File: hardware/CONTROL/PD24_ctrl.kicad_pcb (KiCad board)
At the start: 2 copper layers, 39.7 x 14 mm, 13 parts, among them J1 Conn_01x12_Socket, J2 Conn_01x08_Socket, SW1 SW_Push, SW2 SW_Push, SW3 SW_Push, U1 STM32G031G8Ux, U2 ips_0.96_16080, U3 TPS54202DDC, U4 INA228

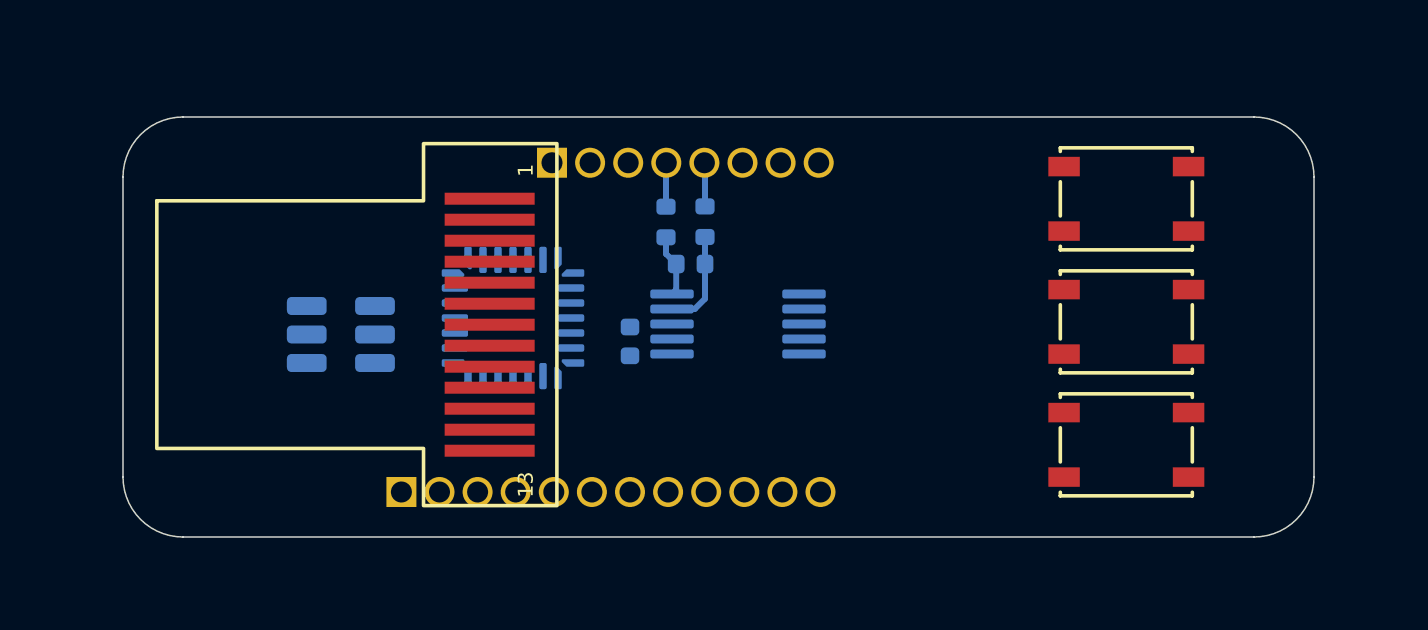
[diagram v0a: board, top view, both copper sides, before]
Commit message: PD24 控制部分的PCB设计完成
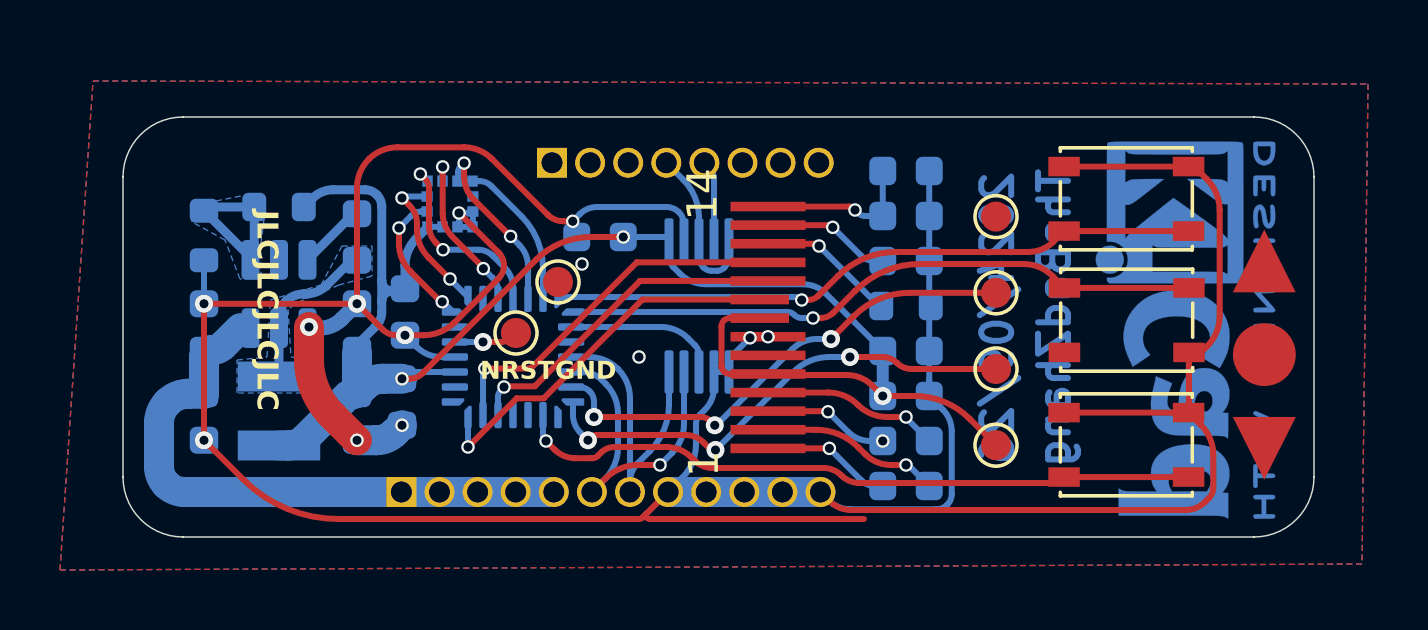
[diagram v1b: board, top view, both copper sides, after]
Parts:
- removed R6: 68R, Resistor_SMD:R_0402_1005Metric
- removed the U2 at (149.8, 113.2)
- removed the U4 at (153.0, 113.2)
- added C1: 0.1uF, Capacitor_SMD:C_0603_1608Metric, B.Cu at (140.3, 110.2)
- added C10: 4.7uF, Capacitor_SMD:C_0603_1608Metric, B.Cu at (158.6, 114.0)
- added C11: 2.2uF, Capacitor_SMD:C_0603_1608Metric, B.Cu at (158.6, 111.0)
- added C12: 4.7uF, Capacitor_SMD:C_0603_1608Metric, B.Cu at (158.6, 108.0)
- added C13: 0.1uF, Capacitor_SMD:C_0603_1608Metric, B.Cu at (158.6, 109.5)
- added C14: 0.1uF, Capacitor_SMD:C_0603_1608Metric, B.Cu at (141.8, 115.8)
- added C16: 100nF, Capacitor_SMD:C_0603_1608Metric, B.Cu at (141.9, 112.8)
- added C2: 10uF, Capacitor_SMD:C_0603_1608Metric, B.Cu at (135.2, 116.2)
- added C3: 0.1uF, Capacitor_SMD:C_0603_1608Metric, B.Cu at (135.2, 113.2)
- added C4: 22uF, Capacitor_SMD:C_0603_1608Metric, B.Cu at (140.3, 116.2)
- added C5: 10uF, Capacitor_SMD:C_0603_1608Metric, B.Cu at (140.3, 113.2)
- added C8: 1uF, Capacitor_SMD:C_0603_1608Metric, B.Cu at (158.6, 117.0)
- added C9: 0.1uF, Capacitor_SMD:C_0603_1608Metric, B.Cu at (158.6, 115.5)
- added L1: 10uH, Inductor_SMD:L_Abracon_ASPI-3012S, B.Cu at (137.7, 116.0)
- added R2: 100K, Resistor_SMD:R_0603_1608Metric, B.Cu at (137.7, 109.2)
- added R4: 22.1K, Resistor_SMD:R_0603_1608Metric, B.Cu at (135.2, 110.2)
- added SYMBOL1: 符号, Symbol:KiCad-Logo2_5mm_Copper, B.Cu at (167.9, 113.3)
- added TP1: TestPoint, TestPoint:TestPoint_Pad_D1.0mm, F.Cu at (161.6, 109.6)
- added TP2: TestPoint, TestPoint:TestPoint_Pad_D1.0mm, F.Cu at (161.6, 112.1)
- added TP3: TestPoint, TestPoint:TestPoint_Pad_D1.0mm, F.Cu at (161.6, 114.7)
- added TP4: TestPoint, TestPoint:TestPoint_Pad_D1.0mm, F.Cu at (161.6, 117.2)
- added TP5: TestPoint, TestPoint:TestPoint_Pad_D1.0mm, F.Cu at (147.0, 111.8)
- added TP6: TestPoint, TestPoint:TestPoint_Pad_D1.0mm, F.Cu at (145.6, 113.5)
- added U1: LIS2DW12, Package_LGA:LGA-12_2x2mm_P0.5mm, B.Cu at (143.4, 109.2)
- added U12: ~, my_footprint:iic_oled_12864_ssd1312_2, F.Cu at (148.1, 113.2)
- added U5: INA228, Package_SO:VSSOP-10_3x3mm_P0.5mm, B.Cu at (151.7, 112.5)
- C6: value C -> 0.1uF; footprint Capacitor_SMD:C_0402_1005Metric -> Capacitor_SMD:C_0603_1608Metric
- C7: value 100nF -> 1uF; footprint Capacitor_SMD:C_0402_1005Metric -> Capacitor_SMD:C_0603_1608Metric
- R8: value 68R -> 560K; footprint Resistor_SMD:R_0402_1005Metric -> Resistor_SMD:R_0603_1608Metric
- moved C7 10.3 mm to (158.6, 118.5), turned to 180 degrees
- moved R8 7.27 mm to (158.6, 112.5), turned to 180 degrees
- moved C6 3.62 mm to (148.4, 110.2), turned to 180 degrees
- moved U4 2.47 mm to (137.7, 112.2), turned to 90 degrees
- moved U2 1.30 mm to (145.5, 114.2), turned to 0 degrees
- moved SW2 0.22 mm to (165.9, 113.0), turned to 180 degrees
- renumbered U1 to U2, U3 to U4
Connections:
- C6 pad 1: /ina226/VSS -> +3V3
- C6 pad 2: /ina226/GND -> GND
- C7 pad 2: Net-(U4-Vin-) -> Net-(U12-C2P)
- J1 pad 6: /SDA -> /I2C2.SDA
- J1 pad 7: /SCL -> /I2C2.SCL
- R8 pad 1: /VIN- -> GND
- R8 pad 2: Net-(U4-Vin-) -> Net-(U12-IREF)
- SW1 pad 1: unconnected-(SW1-Pad1) -> GND
- SW1 pad 2: unconnected-(SW1-Pad2) -> /KEY1
- SW2 pad 1: unconnected-(SW2-Pad1) -> GND
- SW2 pad 2: unconnected-(SW2-Pad2) -> /KEY2
- SW3 pad 1: unconnected-(SW3-Pad1) -> GND
- SW3 pad 2: unconnected-(SW3-Pad2) -> /KEY3
- U2 pad 10: unconnected-(U1-PA4-Pad10) -> /SPI1.NSS
- U2 pad 11: unconnected-(U1-PA5-Pad11) -> /SPI1.CLK
- U2 pad 12: unconnected-(U1-PA6-Pad12) -> /SPI1.MISO
- U2 pad 13: unconnected-(U1-PA7-Pad13) -> /SPI1.MOSI
- U2 pad 14: unconnected-(U1-PB0-Pad14) -> /KEY1
- U2 pad 15: unconnected-(U1-PB1-Pad15) -> /KEY2
- U2 pad 16: unconnected-(U1-PA8-Pad16) -> /~{ALERT}
- U2 pad 18: unconnected-(U1-PA11/PA9-Pad18) -> /I2C2.SCL
- U2 pad 19: unconnected-(U1-PA12/PA10-Pad19) -> /I2C2.SDA
- U2 pad 20: unconnected-(U1-PA13-Pad20) -> /SWDIO
- U2 pad 21: unconnected-(U1-PA14-Pad21) -> /SWCLK
- U2 pad 23: unconnected-(U1-PB3-Pad23) -> /KEY3
- U2 pad 26: unconnected-(U1-PB6-Pad26) -> /ssd1312/SCL
- U2 pad 27: unconnected-(U1-PB7-Pad27) -> /ssd1312/SDA
- U2 pad 28: unconnected-(U1-PB8-Pad28) -> /ssd1312/RES#
- U2 pad 5: unconnected-(U1-PF2-Pad5) -> /NRST
- U2 pad 7: unconnected-(U1-PA1-Pad7) -> /INT2
- U2 pad 8: unconnected-(U1-PA2-Pad8) -> /INT1
- U4 pad 5: Net-(U3-EN) -> unconnected-(U4-EN-Pad5)
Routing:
- net GND: track 0.00 -> 135.9 mm, vias 0 -> 13
- net +3V3: track 0.00 -> 54.9 mm, vias 0 -> 3
- net /KEY3: track 0.00 -> 23.0 mm, vias 0 -> 1
- net /KEY1: track 0.00 -> 21.8 mm, vias 0 -> 1
- net /KEY2: track 0.00 -> 21.4 mm, vias 0 -> 1
- net +20V: track 0.00 -> 20.0 mm
- net /SWDIO: track 0.00 -> 16.7 mm, vias 0 -> 3
- net /SWCLK: track 0.00 -> 16.6 mm, vias 0 -> 3
- net /ssd1312/RES#: track 0.00 -> 12.8 mm, vias 0 -> 1
- net /ssd1312/SDA: track 0.00 -> 12.5 mm, vias 0 -> 1
- net /ssd1312/SCL: track 0.00 -> 11.3 mm, vias 0 -> 1
- net /I2C2.SDA: track 0.00 -> 11.2 mm, vias 0 -> 1
- net /I2C2.SCL: track 0.00 -> 10.3 mm
- net /SPI1.CLK: track 0.00 -> 6.49 mm, vias 0 -> 2
- net /SPI1.MISO: track 0.00 -> 5.99 mm, vias 0 -> 2
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- added copper zone on B.Cu, net GND
- added copper zone on F.Cu, net GND
- added copper zone on B.Cu, net Net-(U4-FB)
- added copper zone on B.Cu, net Net-(U4-SW)
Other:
- board text added: "GND"
- board text added: "JLCJLCJLCJLC"
- board text added: "NRST"
- board text added: "◀ ● ▶"

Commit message: 硬件1.0版本更新
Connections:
- net /ssd1312/RES# renamed /OLED_RST
- net /ssd1312/SCL renamed /I2C1.SCL
- net /ssd1312/SDA renamed /I2C1.SDA
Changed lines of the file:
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@@
 	(net 37 "unconnected-(U2-PC15-Pad2)")
 	(net 38 "unconnected-(U2-PA3-Pad9)")
-	(net 39 "/ssd1312/RES#")
-	(net 40 "/ssd1312/SDA")
+	(net 39 "/OLED_RST")
+	(net 40 "/I2C1.SDA")
 	(net 41 "unconnected-(U2-PA15-Pad22)")
-	(net 42 "/ssd1312/SCL")
+	(net 42 "/I2C1.SCL")
 	(net 43 "/KEY1")
 	(net 44 "/KEY2")
@@
 			(size 0.32 1.95)
 			(layers "F.Cu" "F.Paste" "F.Mask")
-			(net 39 "/ssd1312/RES#")
+			(net 39 "/OLED_RST")
 			(pinfunction "RES#")
 			(pintype "input")
@@
 			(size 0.32 2.5)
 			(layers "F.Cu" "F.Paste" "F.Mask")
-			(net 42 "/ssd1312/SCL")
+			(net 42 "/I2C1.SCL")
 			(pinfunction "SCL")
 			(pintype "input")
@@
 			(size 0.32 2.5)
 			(layers "F.Cu" "F.Paste" "F.Mask")
-			(net 40 "/ssd1312/SDA")
+			(net 40 "/I2C1.SDA")
 			(pinfunction "SDA")
 			(pintype "input")
@@
 			(roundrect_rratio 0.25)
 			(net 24 "/SPI1.NSS")
-			(pinfunction "PA4")
+			(pinfunction "SPI1_NSS")
 			(pintype "bidirectional")
 		)
@@
 			(roundrect_rratio 0.25)
 			(net 21 "/SPI1.CLK")
-			(pinfunction "PA5")
+			(pinfunction "SPI1_SCK")
 			(pintype "bidirectional")
 		)
@@
 			(roundrect_rratio 0.25)
 			(net 22 "/SPI1.MISO")
-			(pinfunction "PA6")
+			(pinfunction "SPI1_MISO")
 			(pintype "bidirectional")
 		)
@@
 			(roundrect_rratio 0.25)
 			(net 23 "/SPI1.MOSI")
-			(pinfunction "PA7")
+			(pinfunction "SPI1_MOSI")
 			(pintype "bidirectional")
 		)
@@
 			(roundrect_rratio 0.25)
 			(net 32 "/I2C2.SCL")
-			(pinfunction "PA11/PA9")
+			(pinfunction "I2C2_SCL")
 			(pintype "bidirectional")
 		)
@@
 			(roundrect_rratio 0.25)
 			(net 35 "/I2C2.SDA")
-			(pinfunction "PA12/PA10")
+			(pinfunction "I2C2_SDA")
 			(pintype "bidirectional")
 		)
@@
 			(roundrect_rratio 0.25)
 			(net 33 "/SWDIO")
-			(pinfunction "PA13")
+			(pinfunction "SYS_SWDIO")
 			(pintype "bidirectional")
 		)
@@
 			(layers "B.Cu" "B.Paste" "B.Mask")
 			(net 34 "/SWCLK")
-			(pinfunction "PA14")
+			(pinfunction "SYS_SWCLK")
 			(pintype "bidirectional")
 			(options
@@
 			(layers "B.Cu" "B.Paste" "B.Mask")
 			(roundrect_rratio 0.25)
-			(net 42 "/ssd1312/SCL")
-			(pinfunction "PB6")
+			(net 42 "/I2C1.SCL")
+			(pinfunction "I2C1_SCL")
 			(pintype "bidirectional")
 		)
@@
 			(layers "B.Cu" "B.Paste" "B.Mask")
 			(roundrect_rratio 0.25)
-			(net 40 "/ssd1312/SDA")
-			(pinfunction "PB7")
+			(net 40 "/I2C1.SDA")
+			(pinfunction "I2C1_SDA")
 			(pintype "bidirectional")
 		)
@@
 			(size 0.136863 0.136863)
 			(layers "B.Cu" "B.Paste" "B.Mask")
-			(net 39 "/ssd1312/RES#")
+			(net 39 "/OLED_RST")
 			(pinfunction "PB8")
 			(pintype "bidirectional")

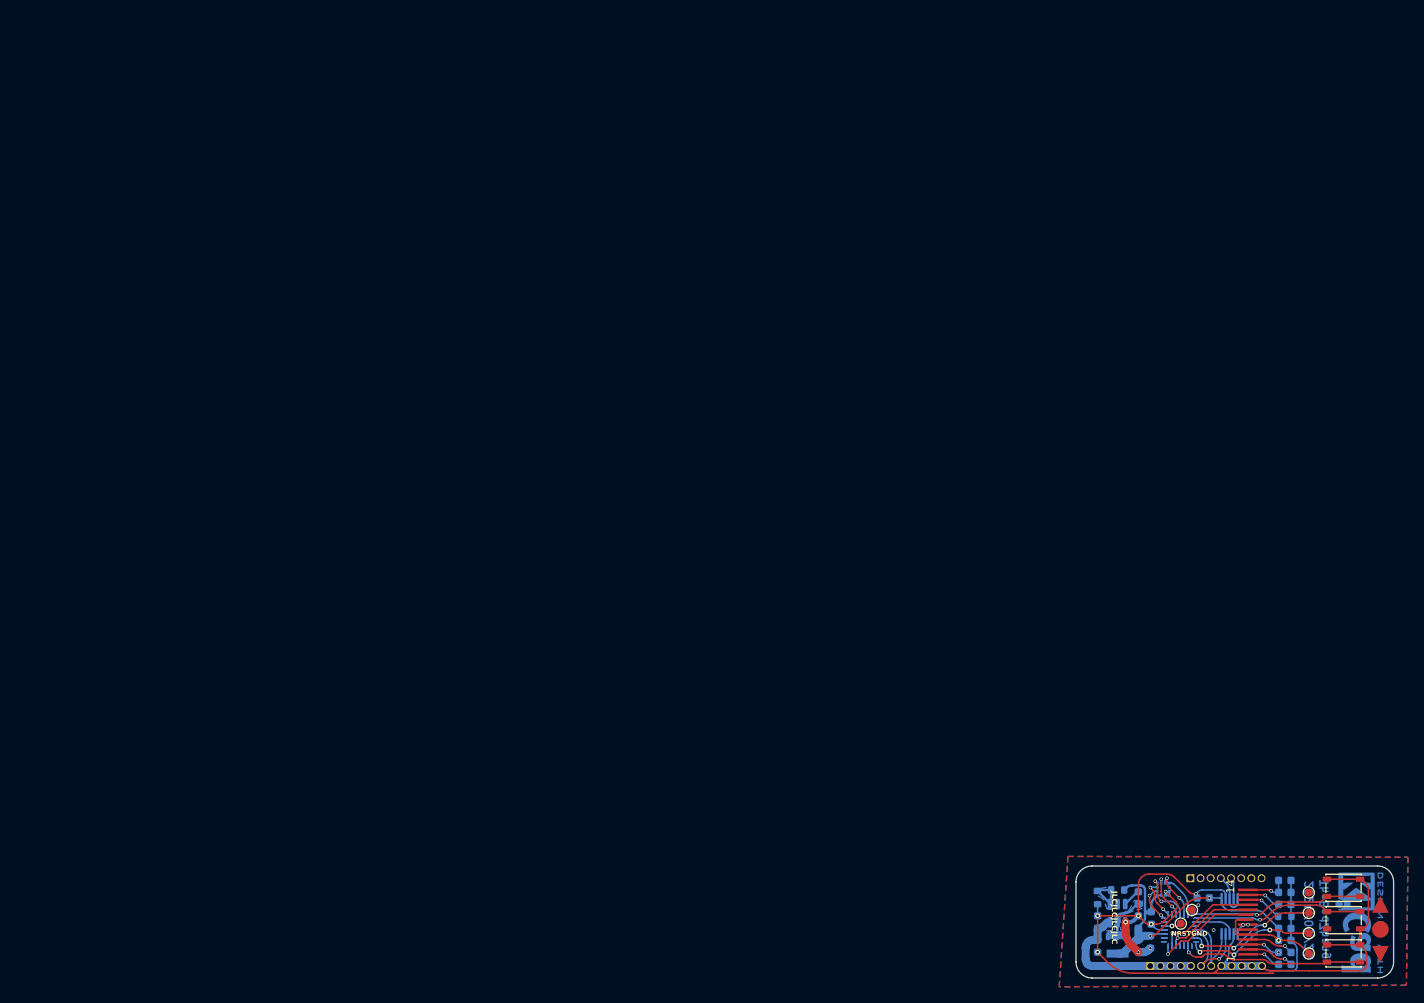
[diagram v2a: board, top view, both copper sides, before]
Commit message: 改变了结构，下沉减少厚度
为了实现这个目标，去掉了按键，将原先的buck电路替换成了ldo，但是会产生0.5W的热功耗，acc也放到了电源板上
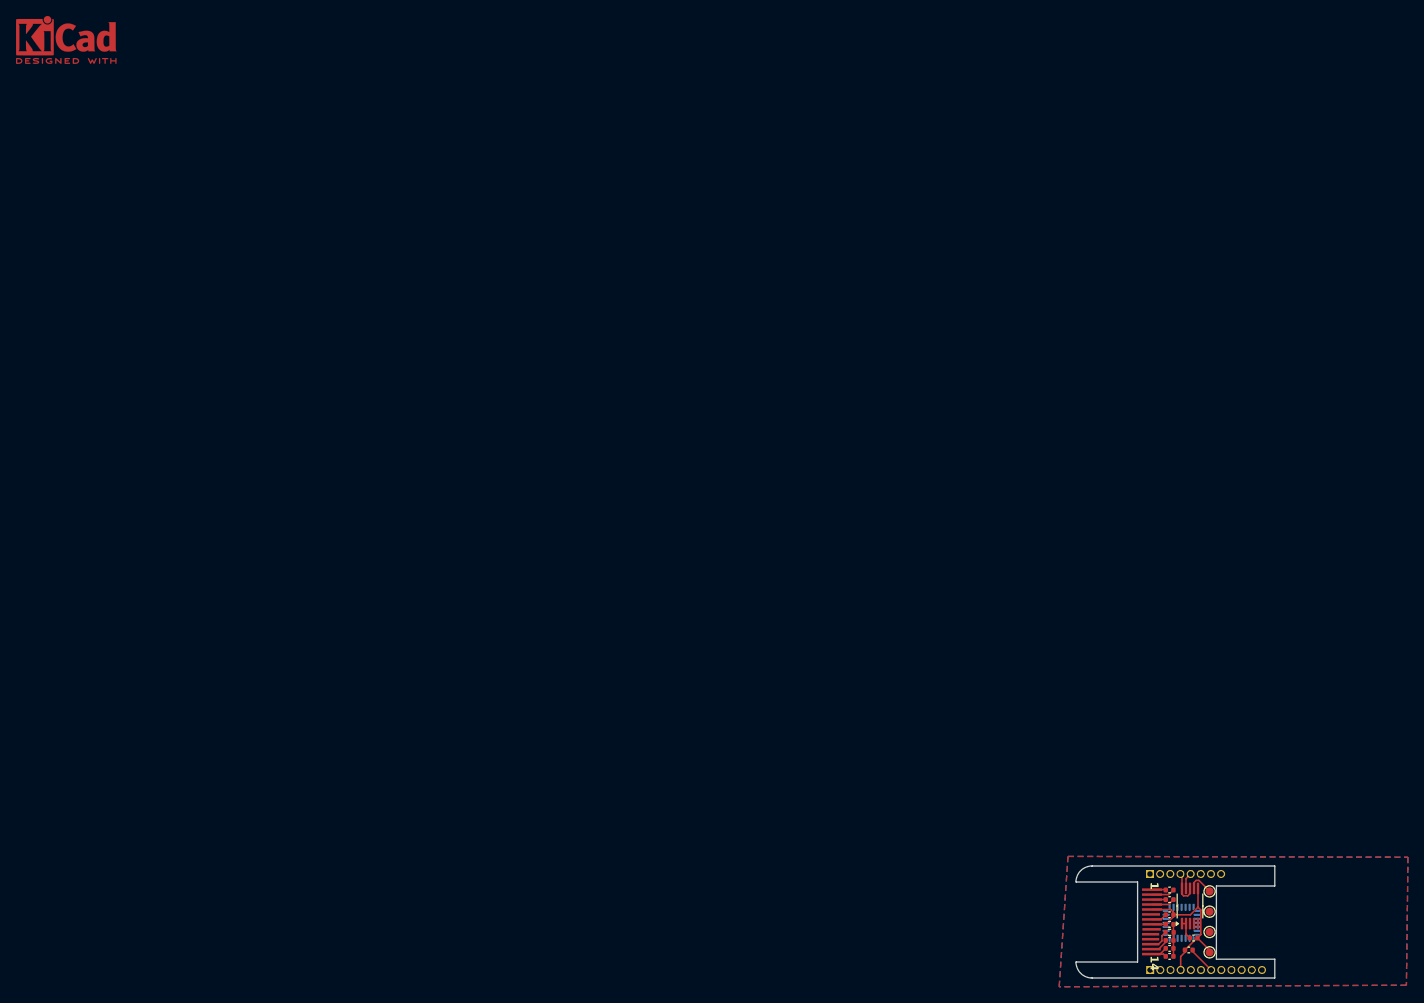
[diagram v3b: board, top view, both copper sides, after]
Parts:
- removed C1, C3: 0.1uF, Capacitor_SMD:C_0603_1608Metric
- removed C16: 100nF, Capacitor_SMD:C_0603_1608Metric
- removed C2, C5: 10uF, Capacitor_SMD:C_0603_1608Metric
- removed C4: 22uF, Capacitor_SMD:C_0603_1608Metric
- removed L1: 10uH, Inductor_SMD:L_Abracon_ASPI-3012S
- removed R2: 100K, Resistor_SMD:R_0603_1608Metric
- removed R4: 22.1K, Resistor_SMD:R_0603_1608Metric
- removed SW1, SW2, SW3: SW_Push, my_footprint:KEY-SMD_4P-L4.2-W3.4-P2.15-LS4.5-TL
- removed TP5, TP6: TestPoint, TestPoint:TestPoint_Pad_D1.0mm
- removed U1: LIS2DW12, Package_LGA:LGA-12_2x2mm_P0.5mm
- removed U4: TPS54202DDC, Package_TO_SOT_SMD:SOT-23-6
- C10, C11, C12, C13, C14, C6, C7, C8, C9: footprint Capacitor_SMD:C_0603_1608Metric -> Capacitor_SMD:C_0402_1005Metric; moved to F.Cu
- R8: footprint Resistor_SMD:R_0603_1608Metric -> Resistor_SMD:R_0402_1005Metric; moved to F.Cu
- SYMBOL1, U5: moved to F.Cu
- moved SYMBOL1 195.7 mm to (6.28, 2.98), turned to 0 degrees
- moved C12 17.3 mm to (144.2, 117.5)
- moved C7 17.1 mm to (144.2, 109.2)
- moved C13 16.0 mm to (144.2, 116.5)
- moved C8 15.8 mm to (144.2, 110.5)
- moved C11 15.1 mm to (144.2, 115.5)
- moved C9 14.8 mm to (144.2, 112.3), turned to 180 degrees
- moved R8 14.5 mm to (144.2, 114.5)
- moved C10 14.4 mm to (144.2, 113.5)
- moved TP1 12.4 mm to (149.2, 109.4)
- moved TP2 12.4 mm to (149.2, 112.0)
- moved TP3 12.4 mm to (149.2, 114.5)
- moved TP4 12.4 mm to (149.2, 117.0)
- moved C6 5.14 mm to (147.2, 115.2)
- moved U5 5.12 mm to (146.8, 111.2)
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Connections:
- J1 pad 1: +20V -> unconnected-(J1-Pin_1-Pad1)
- J1 pad 2: +20V -> unconnected-(J1-Pin_2-Pad2)
- J1 pad 3: +20V -> unconnected-(J1-Pin_3-Pad3)
- J1 pad 4: +20V -> +3V3
- J1 pad 5: +20V -> /I2C2.SDA
- J1 pad 6: /I2C2.SDA -> /I2C2.SCL
- J1 pad 7: /I2C2.SCL -> GND
- U2 pad 1: unconnected-(U2-PC14-Pad1) -> /OLED_RST
- U2 pad 10: /SPI1.NSS -> unconnected-(U2-PA4-Pad10)
- U2 pad 11: /SPI1.CLK -> unconnected-(U2-PA5-Pad11)
- U2 pad 12: /SPI1.MISO -> unconnected-(U2-PA6-Pad12)
- U2 pad 13: /SPI1.MOSI -> unconnected-(U2-PA7-Pad13)
- U2 pad 14: /KEY1 -> unconnected-(U2-PB0-Pad14)
- U2 pad 15: /KEY2 -> unconnected-(U2-PB1-Pad15)
- U2 pad 16: /~{ALERT} -> unconnected-(U2-PA8-Pad16)
- U2 pad 23: /KEY3 -> unconnected-(U2-PB3-Pad23)
- U2 pad 26: /I2C1.SCL -> unconnected-(U2-PB6-Pad26)
- U2 pad 28: /OLED_RST -> /I2C1.SCL
- U2 pad 5: /NRST -> unconnected-(U2-PF2-Pad5)
- U2 pad 7: /INT2 -> unconnected-(U2-PA1-Pad7)
- U2 pad 8: /INT1 -> unconnected-(U2-PA2-Pad8)
- U5 pad 3: /~{ALERT} -> unconnected-(U5-~{Alert}-Pad3)
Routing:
- net GND: track 135.9 -> 15.3 mm, vias 13 -> 0
- net +3V3: track 54.9 -> 23.7 mm, vias 3 -> 0
- net /KEY3: track 23.0 -> 0.00 mm, vias 1 -> 0
- net /KEY1: track 21.8 -> 0.00 mm, vias 1 -> 0
- net /KEY2: track 21.4 -> 0.00 mm, vias 1 -> 0
- net +20V: track 20.0 -> 0.00 mm
- net /SWDIO: track 16.7 -> 0.00 mm, vias 3 -> 0
- net /SWCLK: track 16.6 -> 0.00 mm, vias 3 -> 0
- net /OLED_RST: track 12.8 -> 0.00 mm, vias 1 -> 0
- net /I2C1.SDA: track 12.5 -> 0.00 mm, vias 1 -> 0
- net /I2C1.SCL: track 11.3 -> 0.00 mm, vias 1 -> 0
- net /I2C2.SDA: track 11.2 -> 0.00 mm, vias 1 -> 0
- net /I2C2.SCL: track 10.3 -> 0.00 mm
- net /SPI1.CLK: track 6.49 -> 0.00 mm, vias 2 -> 0
- net /SPI1.MISO: track 5.99 -> 0.00 mm, vias 2 -> 0
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- removed copper zone on B.Cu, net Net-(U4-FB)
- removed copper zone on B.Cu, net Net-(U4-SW)
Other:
- board size 39.7 x 14 mm -> 24.8 x 14 mm
- board text removed: "GND"
- board text removed: "JLCJLCJLCJLC"
- board text removed: "NRST"
- board text removed: "◀ ● ▶"
